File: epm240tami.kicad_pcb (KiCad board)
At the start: 2 copper layers, 25 parts, among them CON1 BARREL_JACK, P1 CONN_01X03, P2 CONN_01X02, P3 CONN_01X03, P4 CONN_02X22, P5 CONN_02X22, P6 JTAG, P7 CONN_01X07, U1 EPM240T100C5N, U2 NCP1117ST33T3G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

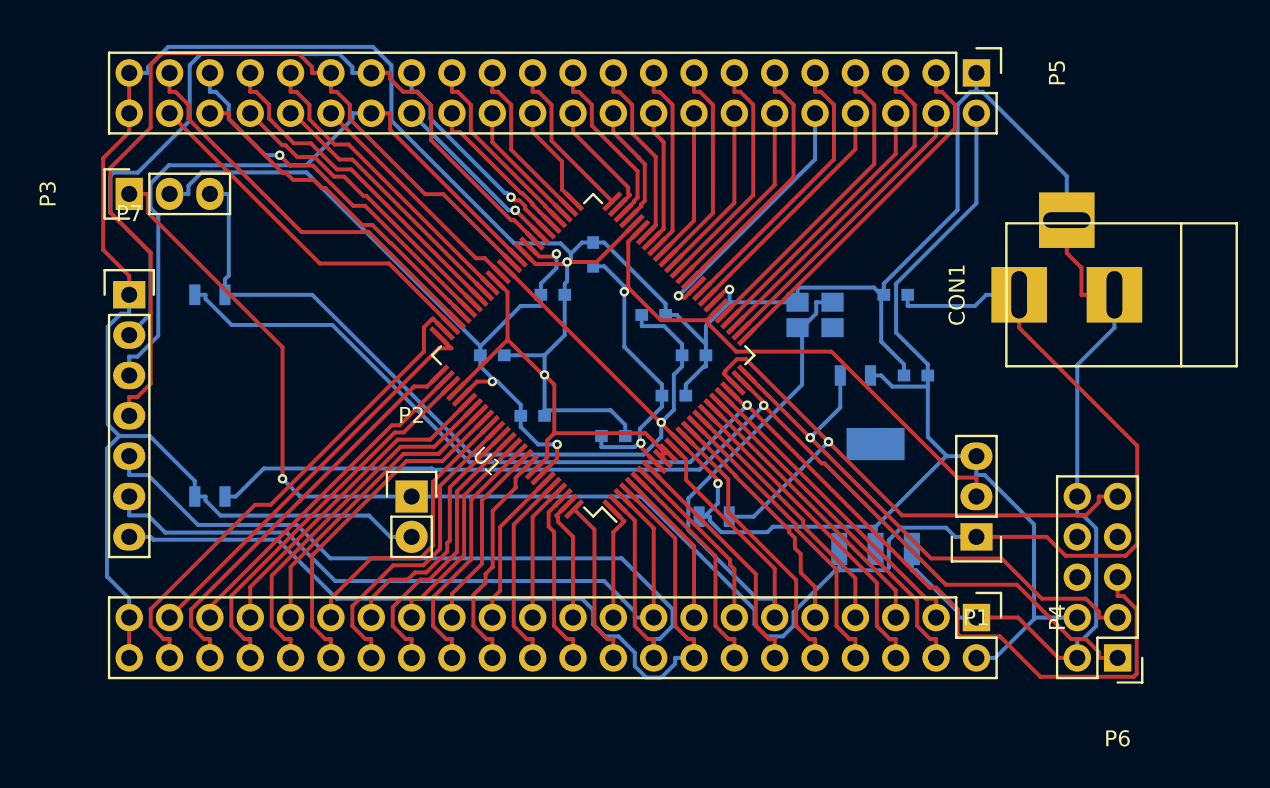
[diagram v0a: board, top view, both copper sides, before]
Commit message: After routing with TopoR and slightly compacting the component layout
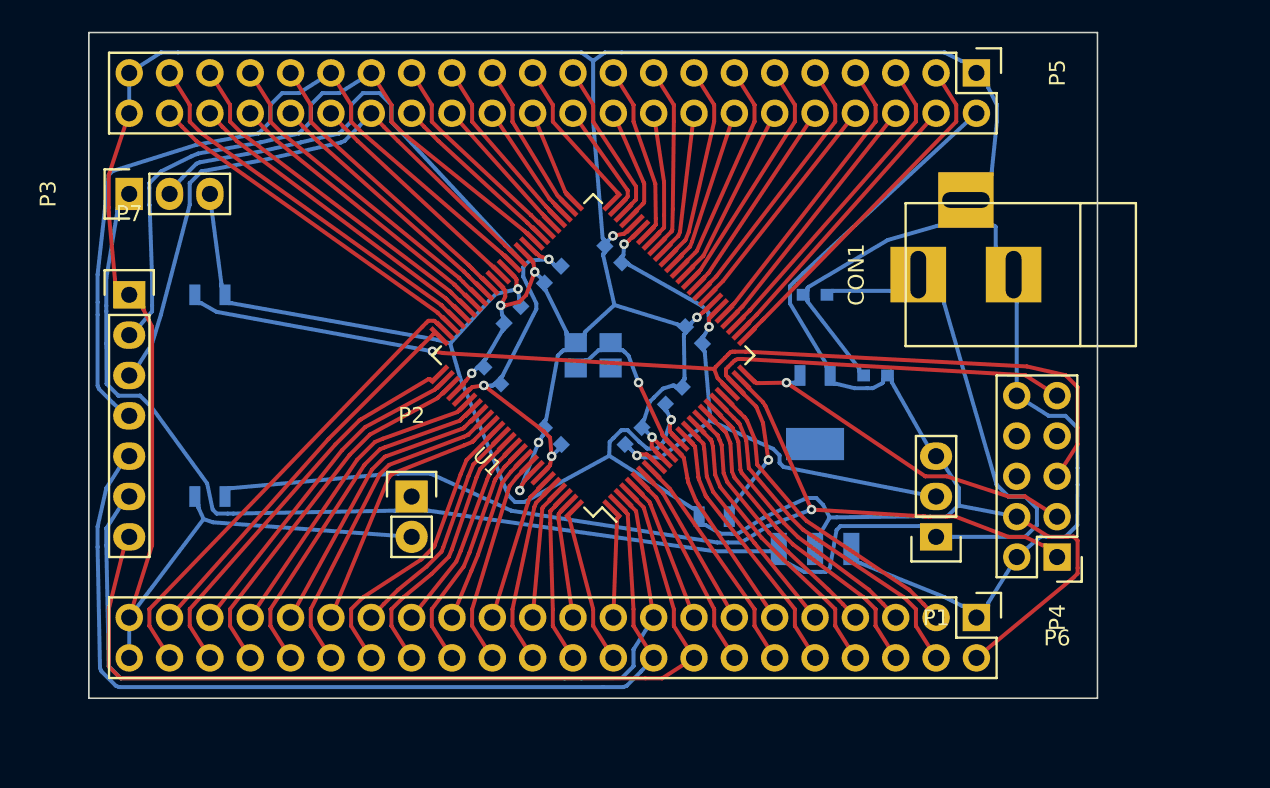
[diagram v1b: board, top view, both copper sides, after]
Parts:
- moved X1 14.2 mm to (157.5, 62.2)
- moved C4 8.89 mm to (152.4, 59.7), turned to 225 degrees
- moved P6 7.41 mm to (186.7, 74.9)
- moved CON1 6.48 mm to (184.2, 57.1)
- moved C1 5.08 mm to (171.4, 58.4)
- moved C6 4.02 mm to (163.8, 61.0), turned to 135 degrees
- moved U2 3.81 mm to (171.4, 71.1)
- moved C3 2.84 mm to (162.6, 64.8), turned to 45 degrees
- moved C2 2.54 mm to (175.3, 63.5)
- moved P1 2.54 mm to (179.1, 73.7)
- moved R4 2.54 mm to (171.4, 63.5)
- moved C10 1.80 mm to (154.9, 67.3), turned to 135 degrees
- moved C5 1.27 mm to (160.0, 67.3), turned to 45 degrees
- moved C7 1.27 mm to (158.8, 55.9), turned to 135 degrees
- moved C8 1.27 mm to (151.1, 63.5), turned to 135 degrees
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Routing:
- net /CLK_CORE: track 40.7 -> 23.3 mm, vias 0 -> 1
- net /TMS: track 81.6 -> 64.9 mm
- net /VCCIO1: track 52.5 -> 40.9 mm, vias 2 -> 3
- net /TDO: track 34.6 -> 23.2 mm
- net /DP1: track 45.4 -> 56.3 mm
- net VCC: track 114.6 -> 104.5 mm, vias 1 -> 0
- net /DI: track 50.2 -> 42.1 mm
- net GND: track 264.5 -> 257.1 mm, vias 3 -> 8
- net /DM: track 53.5 -> 60.4 mm
- net /TDI: track 39.3 -> 32.5 mm
- net /IO62: track 55.1 -> 49.5 mm
- net /VCCIO2: track 49.4 -> 54.5 mm
- net /DO: track 42.9 -> 38.6 mm
- net /DP2: track 53.3 -> 57.4 mm
- net /TCK: track 67.6 -> 64.0 mm
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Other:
- board outline added: 63.5 x 41.9 mm
